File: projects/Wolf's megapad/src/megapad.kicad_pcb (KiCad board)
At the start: 2 copper layers, 127.5 x 54.5 mm, 81 parts, among them SW1 MX1A-11NW, SW2 MX1A-11NW, SW3 MX1A-11NW, SW4 MX1A-11NW, SW5 MX1A-11NW, SW6 MX1A-11NW, U1 SL2.1A_C6798314, U2 TS3USB221RSER, U3 W25Q80DVSNIG, U4 ABM8-272-T3_C20625731, U5 RP2040, U6 NCP1117ST33T3G

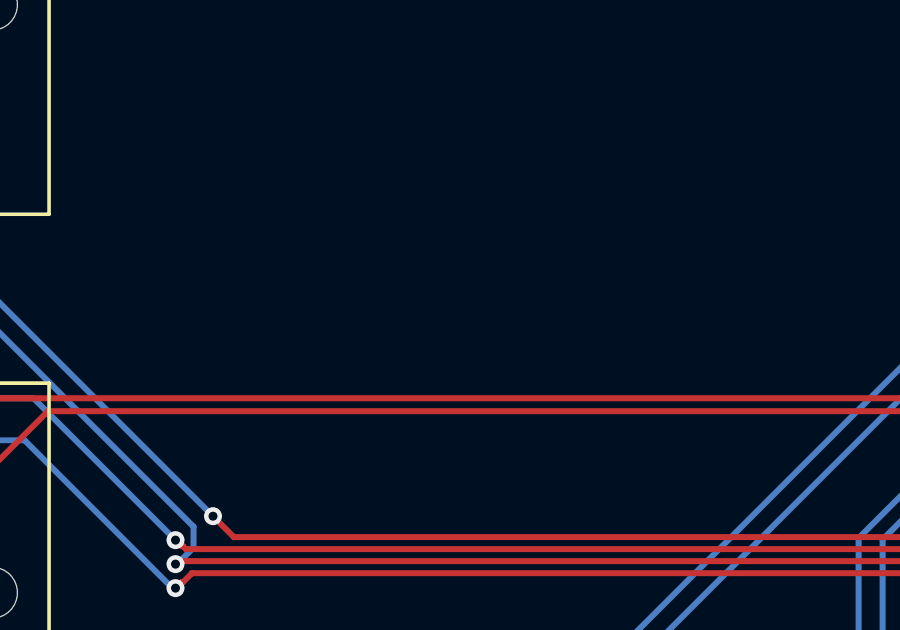
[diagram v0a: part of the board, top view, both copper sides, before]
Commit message: feat: add text and image to PCB
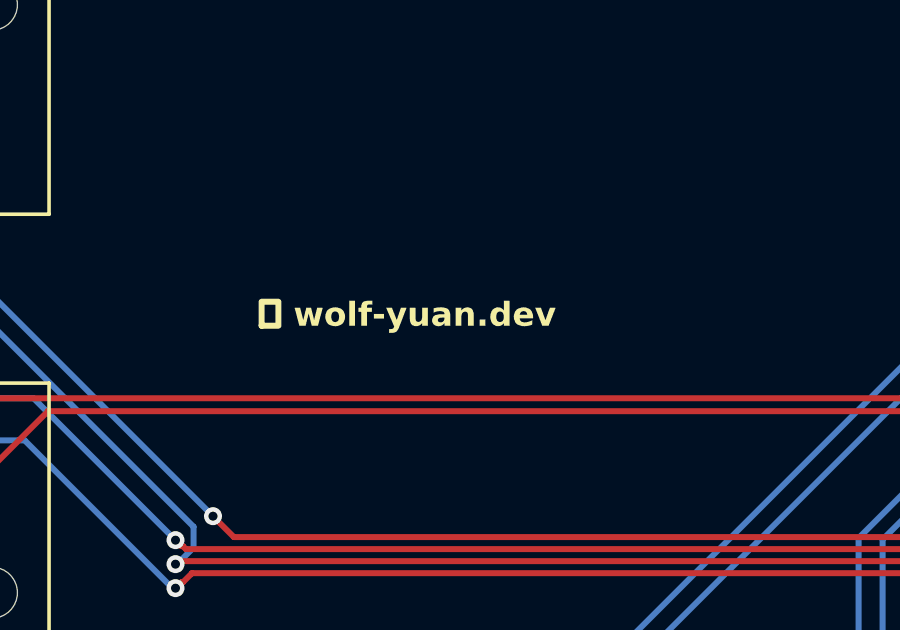
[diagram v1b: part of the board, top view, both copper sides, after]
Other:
- board text added: "Wolf's MegaPad"
- board text added: "󰖟 wolf-yuan.dev"

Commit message: feat: add back image
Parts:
- added G***: LOGO, LOGO, B.Cu at (319.0, 111.0)
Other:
- board text added: "A keyboard with built in USB 2.0 hub, powered by RP2040"

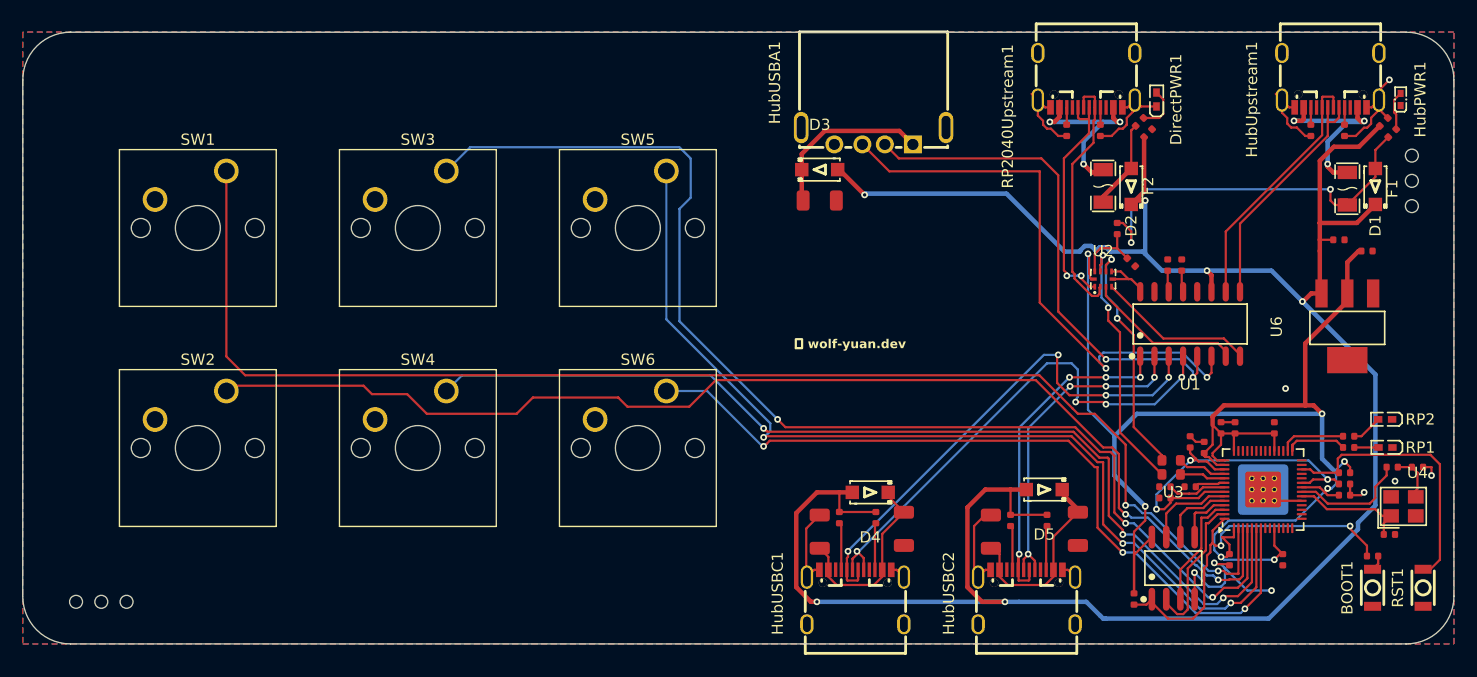
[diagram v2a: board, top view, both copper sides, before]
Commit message: feat: cut down costs and update design files
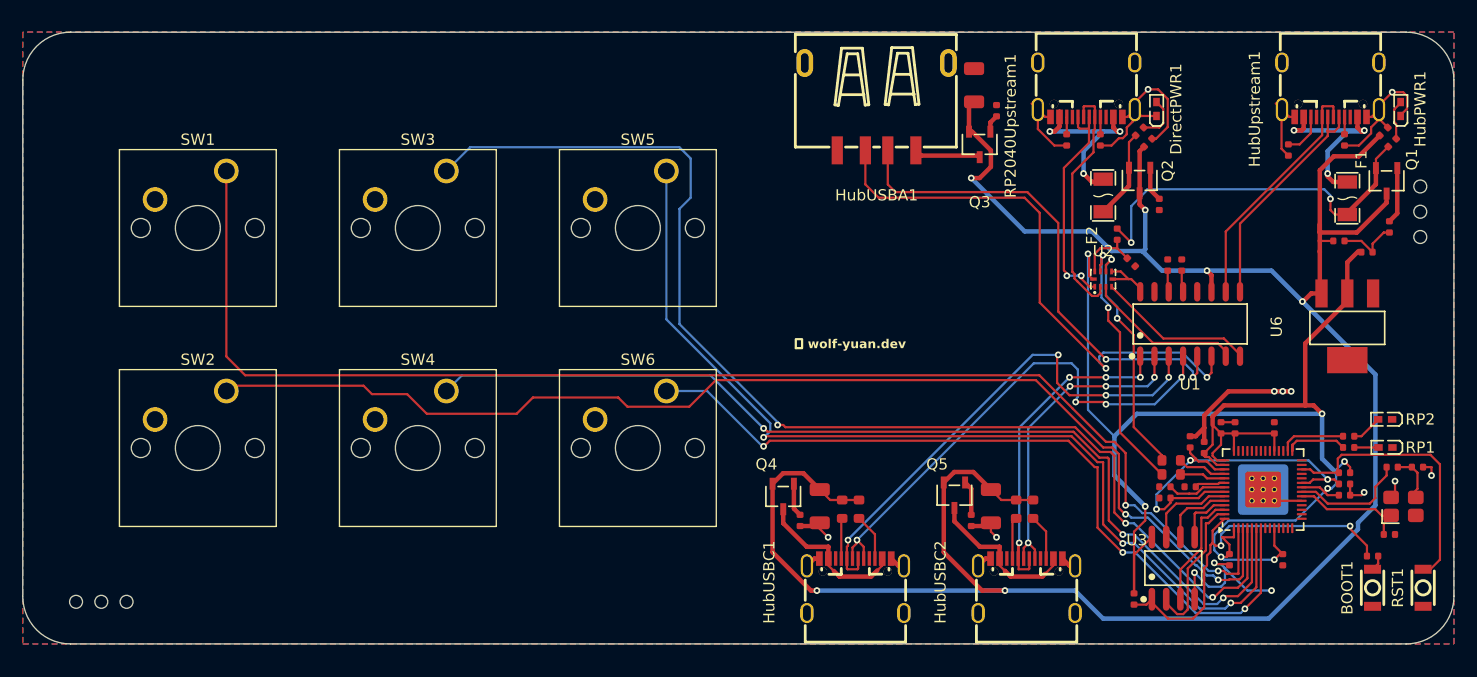
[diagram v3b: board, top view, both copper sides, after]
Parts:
- removed C2, C3: 100uF, PCM_JLCPCB:C_1206
- removed D1, D2, D3, D4, D5: DS34W-MS, easyeda2kicad:SOD-123FL_L2.8-W1.8-LS3.7-RD
- added Q1: AO3415AL, easyeda2kicad:SOT-23-3_L2.9-W1.6-P1.90-LS2.9-BL, F.Cu at (323.0, 103.7)
- added Q2: AO3415AL, easyeda2kicad:SOT-23-3_L2.9-W1.6-P1.90-LS2.9-BL, F.Cu at (301.0, 103.7)
- added Q3: AO3415AL, easyeda2kicad:SOT-23-3_L2.9-W1.6-P1.90-LS2.9-BL, F.Cu at (286.8, 100.5)
- added Q4: AO3415AL, easyeda2kicad:SOT-23-3_L2.9-W1.6-P1.90-LS2.9-BL, F.Cu at (269.2, 131.9)
- added Q5: AO3415AL, easyeda2kicad:SOT-23-3_L2.9-W1.6-P1.90-LS2.9-BL, F.Cu at (284.5, 131.8)
- added R21: 100kΩ, PCM_JLCPCB:R_0402, F.Cu at (323.2, 107.8)
- added R22: 100kΩ, PCM_JLCPCB:R_0402, F.Cu at (302.8, 105.8)
- added R23: 100kΩ, PCM_JLCPCB:R_0402, F.Cu at (288.2, 97.5)
- added R24: 100kΩ, PCM_JLCPCB:R_0402, F.Cu at (270.8, 134.0)
- added R25: 100kΩ, PCM_JLCPCB:R_0402, F.Cu at (286.0, 134.0)
- DirectPWR1: value FC-F1005BK-470G5 -> FC-F1005WD-455K5
- HubPWR1: value FC-F1005UGK-520M5 -> FC-F1005WD-455K5; footprint easyeda2kicad:LED0402-RD -> easyeda2kicad:LED0402-R-RD
- HubUSBA1: footprint easyeda2kicad:USB-A-TH_AF-10.0-HC6.3 -> easyeda2kicad:USB-A-SMD_C39429
- R2, R3, R4, R5: footprint PCM_JLCPCB:R_0402 -> PCM_JLCPCB:R_0603
- U4: value ABM8-272-T3_C20625731 -> X322512MSB4SI; footprint easyeda2kicad:CRYSTAL-SMD_4P-L3.2-W2.5-BL -> PCM_JLCPCB:CRYSTAL-SMD_4P-L3.2-W2.5-BL
- moved C1 17.2 mm to (286.2, 95.2), turned to -90 degrees
- moved C5 8.01 mm to (287.8, 132.7)
- moved C4 7.77 mm to (272.5, 132.7)
- moved ? 2.85 mm to (326.0, 104.2)
- moved ? 2.85 mm to (326.0, 108.8)
- moved REF** 2.85 mm to (326.0, 106.5)
- moved R1 2.66 mm to (314.2, 101.0)
- moved HubUSBA1 2.62 mm to (277.6, 97.1)
- moved G*** 1.75 mm to (319.0, 112.8)
- moved R2 1.68 mm to (276.0, 133.0)
- moved R3 1.60 mm to (291.5, 133.0)
- moved R5 1.12 mm to (290.0, 133.0)
- moved HubUSBC1 1.00 mm to (275.7, 139.8)
- moved HubUSBC2 1.00 mm to (290.9, 139.8)
- moved C11 0.85 mm to (301.8, 100.3)
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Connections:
- C1 pad 2: Net-(D3-K) -> +5V
- C4 pad 2: Net-(D4-K) -> +5V
- C5 pad 2: Net-(D5-K) -> +5V
- HubPWR1 pad 1: GND -> Net-(HubPWR1-A)
- HubPWR1 pad 2: Net-(HubPWR1-A) -> GND
- HubUSBA1 pad 1: Net-(D3-K) -> Net-(HubUSBA1-VCC)
- HubUSBA1 pad 5: GND -> (no net)
- HubUSBA1 pad 6: GND -> (no net)
- HubUSBC1 pad A4: Net-(D4-K) -> Net-(Q4-D)
- HubUSBC1 pad A9: Net-(D4-K) -> Net-(Q4-D)
- HubUSBC2 pad A4: Net-(D5-K) -> Net-(Q5-D)
- HubUSBC2 pad A9: Net-(D5-K) -> Net-(Q5-D)
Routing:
- net GND: track 81.7 -> 106.6 mm, vias 8 -> 13
- net Net-(D5-K): track 17.2 -> 0.00 mm
- net Net-(D4-K): track 17.2 -> 0.00 mm
- net Net-(D3-K): track 15.9 -> 0.00 mm
- net Net-(Q4-D): track 0.00 -> 14.5 mm
- net Net-(Q5-D): track 0.00 -> 14.4 mm
- net Net-(HubUSBA1-VCC): track 0.00 -> 5.94 mm
- net Net-(Q1-G): track 0.00 -> 5.03 mm
- net Net-(Q5-G): track 0.00 -> 3.11 mm
- net Net-(Q2-G): track 0.00 -> 3.10 mm
- net +5V: track 207.1 -> 204.1 mm
- net Net-(Q4-G): track 0.00 -> 3.00 mm
- net Net-(HubUpstream1-CC2): track 1.55 -> 3.87 mm
- net Net-(Q3-G): track 0.00 -> 1.60 mm
- net /HubUSBA1-: track 46.0 -> 44.5 mm
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
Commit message: feat: update megapad design and schematic
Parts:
- removed the C11 at (301.8, 100.3)
- removed DirectPWR1: FC-F1005WD-455K5, easyeda2kicad:LED0402-R-RD
- removed F2: SMD1206P150TF, easyeda2kicad:F1206
- removed Q1, Q2, Q3, Q4, Q5: AO3415AL, easyeda2kicad:SOT-23-3_L2.9-W1.6-P1.90-LS2.9-BL
- removed the R11 at (297.5, 100.1)
- removed the R12 at (299.0, 108.5)
- removed the R13 at (301.0, 99.3)
- removed the R14 at (300.2, 111.0)
- removed R21, R22, R23, R24, R25: 100kΩ, PCM_JLCPCB:R_0402
- removed the R8 at (294.5, 100.1)
- removed RP2040Upstream1: USB3.1C16PFSMT, easyeda2kicad:USB-C-SMD_TYPE-C-USB-17
- removed the U2 at (297.8, 112.5)
- added D1: TPD2E2U06DCKR, easyeda2kicad:SC-70-3_L2.0-W1.3-P0.65-LS2.1-BL, F.Cu at (316.6, 100.9)
- added D2: TPD2E2U06DCKR, easyeda2kicad:SC-70-3_L2.0-W1.3-P0.65-LS2.1-BL, F.Cu at (298.6, 105.0)
- added D3: TPD2E2U06DCKR, easyeda2kicad:SC-70-3_L2.0-W1.3-P0.65-LS2.1-BL, F.Cu at (287.8, 134.2)
- added D4: TPD2E2U06DCKR, easyeda2kicad:SC-70-3_L2.0-W1.3-P0.65-LS2.1-BL, F.Cu at (281.0, 104.5)
- HubUSBA1: value AF 10.0 HC6.3 -> USB-AF-90-10X14.4-H6.57
- HubUSBC1, HubUSBC2, HubUpstream1: value USB3.1C16PFSMT -> MC-311D; footprint easyeda2kicad:USB-C-SMD_TYPE-C-USB-17 -> easyeda2kicad:USB-C-SMD_MC-311D
- R14: renamed from R19; value 200Ω -> 47Ω; footprint PCM_JLCPCB:R_0402 -> PCM_JLCPCB:R_0603
- R15: renamed from R20; value 200Ω -> 47Ω; footprint PCM_JLCPCB:R_0402 -> PCM_JLCPCB:R_0603
- R7: value 200Ω -> 150Ω; footprint PCM_JLCPCB:R_0402 -> PCM_JLCPCB:R_0805
- U3: renamed from U4; value X322512MSB4SI -> ABM8-272-T3_C20625731; footprint PCM_JLCPCB:CRYSTAL-SMD_4P-L3.2-W2.5-BL -> easyeda2kicad:CRYSTAL-SMD_4P-L3.2-W2.5-BL
- moved HubUSBC1 44.5 mm to (281.3, 95.7), turned to 180 degrees
- moved SW2 34.5 mm to (248.0, 102.8)
- moved R2 32.4 mm to (282.5, 101.2), turned to 90 degrees
- moved R5 32.2 mm to (279.6, 101.2), turned to 90 degrees
- moved C4 32.0 mm to (284.5, 103.0), turned to -90 degrees
- moved SW3 28.3 mm to (267.5, 102.8)
- moved SW5 22.4 mm to (248.0, 122.5)
- moved HubUSBA1 21.0 mm to (298.6, 97.1)
- moved C1 20.5 mm to (305.0, 103.5), turned to 90 degrees
- moved ? 19.6 mm to (309.0, 94.5), turned to 180 degrees
- moved REF** 19.0 mm to (311.2, 94.5), turned to 180 degrees
- moved ? 19.0 mm to (313.5, 94.5), turned to 180 degrees
- moved ? 11.0 mm to (217.2, 141.0)
- moved ? 11.0 mm to (221.8, 141.0)
- moved REF** 11.0 mm to (219.5, 141.0)
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- renumbered C14 to C11, C15 to C12, C16 to C13, C17 to C14, C18 to C15, C19 to C16, C20 to C17, C21 to C18, C22 to C19, C6 to C2, C23 to C20, C24 to C21, C25 to C22, C7 to C3, C8 to C6, C12 to C7, C9 to C8, C13 to C9, R15 to R10, R16 to R11, R17 to R12, R18 to R13, R6 to R4, R4 to R5, R5 to R6, R9 to R8, R10 to R9, U6 to U2, U3 to U4
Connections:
- F1 pad 2: /5VDET -> +5V
- HubUSBA1 pad 1: Net-(HubUSBA1-VCC) -> +5V
- HubUSBA1 pad 5: (no net) -> GND
- HubUSBA1 pad 6: (no net) -> GND
- R1 pad 2: Net-(HubUpstream1-CC2) -> Net-(HubUpstream1-CC1)
- R11 pad 1: Net-(U2-D+) -> /HubRP2040+
- R12 pad 1: Net-(U2-D-) -> /HubRP2040-
- R2 pad 2: Net-(HubUSBC1-CC2) -> Net-(HubUSBC1-CC1)
- R3 pad 2: Net-(HubUSBC2-CC2) -> Net-(HubUSBC2-CC1)
- R4 pad 2: Net-(HubUpstream1-CC1) -> Net-(HubUpstream1-CC2)
- R5 pad 2: Net-(HubUSBC1-CC1) -> Net-(HubUSBC1-CC2)
- R6 pad 2: Net-(HubUSBC2-CC1) -> Net-(HubUSBC2-CC2)
- R7 pad 1: /5VDET -> +5V
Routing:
- net GND: track 106.6 -> 53.6 mm, vias 13 -> 11
- net /5VDET: track 34.4 -> 0.00 mm, vias 2 -> 0
- net +5V: track 204.1 -> 170.5 mm, vias 6 -> 8
- net Net-(U5-GPIO2): track 107.3 -> 77.6 mm, vias 3 -> 2
- net Net-(U2-D+): track 23.3 -> 0.00 mm, vias 2 -> 0
- net /DirectD-: track 21.8 -> 0.00 mm
- net Net-(U2-D-): track 21.5 -> 0.00 mm, vias 2 -> 0
- net +3V3: track 154.6 -> 133.9 mm, vias 7 -> 8
- net /DirectD+: track 20.2 -> 0.00 mm, vias 2 -> 0
- net /HubUSBA1+: track 50.4 -> 31.9 mm
- net /VBUSDirect: track 17.1 -> 0.00 mm, vias 3 -> 0
- net Net-(Q4-D): track 14.5 -> 0.00 mm
- net Net-(Q5-D): track 14.4 -> 0.00 mm
- net /HubUSBA1-: track 44.5 -> 30.2 mm
- net Net-(U5-GPIO3): track 89.6 -> 101.4 mm, vias 3 -> 2
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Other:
- board size 127.5 x 54.5 mm -> 117.3 x 54.5 mm
- board text added: "1.1V"
- board text added: "1.8V"
- board text added: "3.3V"
- board text added: "5V"
- board text added: "GPIO0"
- board text added: "GPIO1"
- board text added: "GPIO2"
- board text added: "GPIO3"
- board text added: "GPIO4"
- board text added: "GPIO5"
- board text added: "USBA Out"
- board text added: "USBC Out1"
- board text added: "USBC Out2"
- board text added: "USBC Source"
- board text removed: "Wolf's MegaPad"
- board text removed: "󰖟 wolf-yuan.dev"
